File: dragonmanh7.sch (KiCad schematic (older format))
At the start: 113 parts, among them J1 USB_B, J10 Conn_02x12_Odd_Even, J11 Conn_02x03_Odd_Even, J12 VBAT+, J13 Conn_02x05_Odd_Even, J14 VBATG, J15 Conn_02x02_Odd_Even, J18 Conn_02x05_Odd_Even, J2 73725-0110BLF, J3 RJ45_Amphenol_RJMG1BD3B8K1ANR, J4 Micro_SD_Card, J5 Screw_Terminal_01x06, J6 Conn_02x12_Odd_Even, J7 USB_B, J8 Screw_Terminal_01x02, J9 Conn_02x12_Odd_Even, SW1 RESET, SW2 PC13, U1 STM32H743VITx, U10 USBLC6-2SC6, U12 TCAN332, U13 ISL83483, U14 MIC2005A, U2 KSZ8081RNA, U5 S25FL127SABMFI101, U6 AP63203, U7 USBLC6-2SC6, U8 STM32F042F6Px, U9 USBLC6-2SC6, Y1 8MHz, Y2 32.768KHz, Y3 25MHz

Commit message: Add voltage testpoints
Signed-off-by: Martin Alejandro Ribelotta <martinribelotta@gmail.com>
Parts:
- added TP1: VBAT_TP, TestPoint:TestPoint_Pad_D2.5mm, symbol Connector:TestPoint_Probe
- added TP2: VBUS1_TP, TestPoint:TestPoint_Pad_D2.5mm, symbol Connector:TestPoint_Probe
- added TP3: VBUS2_TP, TestPoint:TestPoint_Pad_D2.5mm, symbol Connector:TestPoint_Probe
- added TP4: VBUS3_TP, TestPoint:TestPoint_Pad_D2.5mm, symbol Connector:TestPoint_Probe
- added TP5: VIN_TP, TestPoint:TestPoint_Pad_D2.5mm, symbol Connector:TestPoint_Probe
- added TP6: 3V3_TP, TestPoint:TestPoint_Pad_D2.5mm, symbol Connector:TestPoint_Probe
- U8: symbol dragonmanh7-rescue:STM32F042F4Px-MCU_ST_STM32F0 -> dragonmanh7-rescue:STM32F042F4Px-MCU_ST_STM32F0-dragonmanh7-rescue
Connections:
- wire segments 246 -> 252
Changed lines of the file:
@@
 	1250 8400 1350 8400
 $Comp
-L dragonmanh7-rescue:STM32F042F4Px-MCU_ST_STM32F0 U8
+L dragonmanh7-rescue:STM32F042F4Px-MCU_ST_STM32F0-dragonmanh7-rescue U8
 U 1 1 5C7F1703
 P 14650 1800
@@
 	1    0    0    -1
 $EndComp
+$Comp
+L Connector:TestPoint_Probe TP6
+U 1 1 5E1CFBDB
+P 15200 8200
+F 0 "TP6" H 15352 8301 50  0000 L CNN
+F 1 "3V3_TP" H 15352 8210 50  0000 L CNN
+F 2 "TestPoint:TestPoint_Pad_D2.5mm" H 15400 8200 50  0001 C CNN
+F 3 "~" H 15400 8200 50  0001 C CNN
+	1    15200 8200
+	1    0    0    -1
+$EndComp
+Connection ~ 15100 8200
+Wire Wire Line
+	15100 8200 15200 8200
+$Comp
+L Connector:TestPoint_Probe TP5
+U 1 1 5E1E58CC
+P 14000 8050
+F 0 "TP5" H 14153 8151 50  0000 L CNN
+F 1 "VIN_TP" H 14153 8060 50  0000 L CNN
+F 2 "TestPoint:TestPoint_Pad_D2.5mm" H 14200 8050 50  0001 C CNN
+F 3 "~" H 14200 8050 50  0001 C CNN
+	1    14000 8050
+	1    0    0    -1
+$EndComp
+Wire Wire Line
+	14000 8050 13850 8050
+$Comp
+L Connector:TestPoint_Probe TP3
+U 1 1 5E1FA9DD
+P 7950 4850
+F 0 "TP3" H 8005 5140 50  0000 C CNN
+F 1 "VBUS2_TP" H 8005 5049 50  0000 C CNN
+F 2 "TestPoint:TestPoint_Pad_D2.5mm" H 8150 4850 50  0001 C CNN
+F 3 "~" H 8150 4850 50  0001 C CNN
+	1    7950 4850
+	-1   0    0    -1
+$EndComp
+Wire Wire Line
+	7950 4850 8300 4850
+$Comp
+L Connector:TestPoint_Probe TP2
+U 1 1 5E213482
+P 7950 3600
+F 0 "TP2" H 8005 3890 50  0000 C CNN
+F 1 "VBUS1_TP" H 8005 3799 50  0000 C CNN
+F 2 "TestPoint:TestPoint_Pad_D2.5mm" H 8150 3600 50  0001 C CNN
+F 3 "~" H 8150 3600 50  0001 C CNN
+	1    7950 3600
+	-1   0    0    -1
+$EndComp
+Wire Wire Line
+	8350 3600 7950 3600
+$Comp
+L Connector:TestPoint_Probe TP4
+U 1 1 5E228BB0
+P 8050 6400
+F 0 "TP4" H 8203 6408 50  0000 L CNN
+F 1 "VBUS3_TP" H 8203 6499 50  0000 L CNN
+F 2 "TestPoint:TestPoint_Pad_D2.5mm" H 8250 6400 50  0001 C CNN
+F 3 "~" H 8250 6400 50  0001 C CNN
+	1    8050 6400
+	-1   0    0    1
+$EndComp
+Wire Wire Line
+	8050 6400 8400 6400
+$Comp
+L Connector:TestPoint_Probe TP1
+U 1 1 5E2616EE
+P 1000 5400
+F 0 "TP1" H 1055 5690 50  0000 C CNN
+F 1 "VBAT_TP" H 1055 5599 50  0000 C CNN
+F 2 "TestPoint:TestPoint_Pad_D2.5mm" H 1200 5400 50  0001 C CNN
+F 3 "~" H 1200 5400 50  0001 C CNN
+	1    1000 5400
+	-1   0    0    -1
+$EndComp
+$Comp
+L power:+BATT #PWR0127
+U 1 1 5E26B945
+P 1150 5400
+F 0 "#PWR0127" H 1150 5250 50  0001 C CNN
+F 1 "+BATT" V 1165 5527 50  0000 L CNN
+F 2 "" H 1150 5400 50  0001 C CNN
+F 3 "" H 1150 5400 50  0001 C CNN
+	1    1150 5400
+	0    1    1    0
+$EndComp
+Wire Wire Line
+	1150 5400 1000 5400
 $EndSCHEMATC

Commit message: Change PHY to LAN8742 and change power scheme to improve 5V handling
Signed-off-by: Martin Ribelotta <martinribelotta@gmail.com>
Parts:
- removed J1, J7: USB_B, Connector_USB:USB_B_OST_USB-B1HSxx_Horizontal, symbol Connector:USB_B
- removed J11: Conn_02x03_Odd_Even, Connector_PinHeader_2.54mm:PinHeader_2x03_P2.54mm_Vertical, symbol Connector_Generic:Conn_02x03_Odd_Even
- removed U2: KSZ8081RNA, Package_DFN_QFN:QFN-24-1EP_4x4mm_P0.5mm_EP2.6x2.6mm, symbol Interface_Ethernet:KSZ8081RNA
- added C36: 0.1u, Capacitor_SMD:C_0603_1608Metric, symbol Device:C_Small
- added C37, C38: 2.2u, Capacitor_SMD:C_0805_2012Metric, symbol Device:C_Small
- added D3: ABS6UTR, Diode_SMD:Diode_Bridge_Diotec_ABS, symbol Diode_Bridge:ABS2
- added FB1: Ferrite_Bead, Inductor_SMD:L_0603_1608Metric, symbol Device:Ferrite_Bead
- added J1, J7: USB_C, Connector_USB:USB_C_Receptacle_Palconn_UTC16-G, symbol Connector:USB_C_Receptacle_USB2.0
- added J11: Conn_02x05_Odd_Even, Connector_PinSocket_2.54mm:PinSocket_2x05_P2.54mm_Vertical, symbol Connector_Generic:Conn_02x05_Odd_Even
- added JP3: BOOTB, Connector_PinHeader_2.54mm:PinHeader_1x02_P2.54mm_Vertical, symbol Device:Jumper_NC_Small
- added R25, R27, R29: 33R, Resistor_SMD:R_0603_1608Metric, symbol Device:R_Small
- added R26, R28, R30, R31, R36: 10K, Resistor_SMD:R_0603_1608Metric, symbol Device:R_Small
- added R32, R33, R34, R35: 49.9R, Resistor_SMD:R_0603_1608Metric, symbol Device:R_Small
- added R37: 220R, Resistor_SMD:R_0603_1608Metric, symbol Device:R_Small
- added R38, R39, R40, R41: 5K1, Resistor_SMD:R_0603_1608Metric, symbol Device:R_Small
- added TP7: M0-SWDIO, TestPoint:TestPoint_Pad_1.0x1.0mm, symbol Connector:TestPoint_Probe
- added TP8: M0-SWCLK, TestPoint:TestPoint_Pad_1.0x1.0mm, symbol Connector:TestPoint_Probe
- added TP9: M0-RST, TestPoint:TestPoint_Pad_1.0x1.0mm, symbol Connector:TestPoint_Probe
- added U2: LAN8742A-CZ-TR, footprints:Microchip-C04-143B-S4QFN-0-0-IPC_C, symbol eec:LAN8742A-CZ-TR
- added U3: AZ1117CD-3.3TRG1, Package_TO_SOT_SMD:TO-252-2, symbol Regulator_Linear:AZ1117-3.3
- C1, C10, C11, C12, C13, C14, C15, C16, C2, C20, C21, C22, C23, C24, C25, C26, C27, C28, C3, C34, C4, C43, C6, C7, C8, C9: footprint Capacitor_SMD:C_0805_2012Metric -> Capacitor_SMD:C_0603_1608Metric
- C18: value 4.7u -> 470p; footprint Capacitor_SMD:C_0805_2012Metric -> Capacitor_SMD:C_0603_1608Metric
- C19, C5: value 4.7u -> 10u
- C32, C33: value 22p -> 30p; footprint Capacitor_SMD:C_0805_2012Metric -> Capacitor_SMD:C_0603_1608Metric
- C35: value 0.1u -> 22n; footprint Capacitor_SMD:C_0805_2012Metric -> Capacitor_SMD:C_0603_1608Metric
- D2, D4, D5: value B120-E3 -> MBR120VLSFT3G; footprint Diode_SMD:D_SOD-123 -> Diode_SMD:D_SOD-123F
- L1: value 68uH -> 4.7u; manf# 1255AY-3R9N=P3 -> 1255AY-4R7M=P3
- R1, R10, R11, R12, R13, R14, R15, R16, R17, R18, R19, R2, R20, R21, R22, R23, R24, R3, R7, R8, R9: footprint Resistor_SMD:R_0805_2012Metric -> Resistor_SMD:R_0603_1608Metric
- R4: value 4K7 -> 33R; footprint Resistor_SMD:R_0805_2012Metric -> Resistor_SMD:R_0603_1608Metric; manf# RC0805JR-074K7L -> CRGCQ0805J22R
- R5: value 4K7 -> 10K; footprint Resistor_SMD:R_0805_2012Metric -> Resistor_SMD:R_0603_1608Metric
- R6: value 6.49K 1% -> 12K1; footprint Resistor_SMD:R_0805_2012Metric -> Resistor_SMD:R_0603_1608Metric
- U10, U7, U9: symbol Power_Protection:USBLC6-2SC6 -> dragonmanh7-rescue:USBLC6-2SC6-Power_Protection
- U6: value AP63203 -> AP63205
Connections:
- net labels added: +5V, 1V8ETH, PHY_CRS_DV, PHY_RXD0, PHY_RXD1, VDDETH, VDINA, VDINB, ~ETH_RST
- net labels removed: ETH_LED
- wire segments 252 -> 364
- no-connect marks 8 -> 10
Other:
- moved on the sheet: C17, C18, C19, C20, C21, C23, C28, C29, C30, C31, C32, C33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

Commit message: Improve schematic and PCB
Signed-off-by: Martin Ribelotta <martinribelotta@gmail.com>
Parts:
- added J16: Conn_02x02_Odd_Even, Connector_PinSocket_2.54mm:PinSocket_2x02_P2.54mm_Vertical, symbol Connector_Generic:Conn_02x02_Odd_Even
- added TP10: VDC_TP, TestPoint:TestPoint_Pad_D2.5mm, symbol Connector:TestPoint_Probe
- added TP11: 5V_TP, TestPoint:TestPoint_Pad_D2.5mm, symbol Connector:TestPoint_Probe
- J1, J7: symbol Connector:USB_C_Receptacle_USB2.0 -> dragonmanh7-rescue:USB_C_Receptacle_USB2.0-Connector
- J6: footprint Connector_PinSocket_2.54mm:PinSocket_2x12_P2.54mm_Vertical -> Connector_PinSocket_2.54mm:PinSocket_2x08_P2.54mm_Vertical; symbol Connector_Generic:Conn_02x12_Odd_Even -> Connector_Generic:Conn_02x08_Odd_Even
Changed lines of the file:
@@
 Text Label 3750 6250 0    50   ~ 0
 PC13
-Text Label 1150 10000 2    50   ~ 0
+Text Label 1150 9900 2    50   ~ 0
 PD8
-Text Label 1650 10000 0    50   ~ 0
+Text Label 1650 9900 0    50   ~ 0
 PD9
-Text Label 1150 10100 2    50   ~ 0
+Text Label 1150 10000 2    50   ~ 0
 PD10
-Text Label 1650 10100 0    50   ~ 0
+Text Label 1650 10000 0    50   ~ 0
 PD11
-Text Label 1150 10200 2    50   ~ 0
+Text Label 1150 10100 2    50   ~ 0
 PD12
-Text Label 1650 10200 0    50   ~ 0
+Text Label 1650 10100 0    50   ~ 0
 PD13
-Text Label 1150 10300 2    50   ~ 0
+Text Label 1150 10200 2    50   ~ 0
 PD14
-Text Label 1650 10300 0    50   ~ 0
+Text Label 1650 10200 0    50   ~ 0
 PD15
-Text Label 1150 10400 2    50   ~ 0
+Text Label 1150 10300 2    50   ~ 0
 PC6
-Text Label 1650 10400 0    50   ~ 0
+Text Label 1650 10300 0    50   ~ 0
 PC7
-Text Label 1150 10500 2    50   ~ 0
+Text Label 1150 10400 2    50   ~ 0
 PC9
-Text Label 1650 10500 0    50   ~ 0
+Text Label 1650 10400 0    50   ~ 0
 PA8
-Text Label 1650 9900 0    50   ~ 0
+Text Label 1650 9800 0    50   ~ 0
 PB10
 Text Label 1150 9700 2    50   ~ 0
-PE11
-Text Label 1650 9700 0    50   ~ 0
-PE12
-Text Label 1150 9800 2    50   ~ 0
 PE13
-Text Label 1650 9800 0    50   ~ 0
+Text Label 1650 9700 0    50   ~ 0
 PE14
-Text Label 1150 9900 2    50   ~ 0
+Text Label 1150 9800 2    50   ~ 0
 PE15
-Wire Wire Line
-	1150 9600 1150 9500
-Wire Wire Line
-	1650 9500 1650 9600
-$Comp
-L power:GND #PWR0151
-U 1 1 5C757D5C
-P 1150 9600
-F 0 "#PWR0151" H 1150 9350 50  0001 C CNN
-F 1 "GND" V 1150 9450 50  0000 R CNN
-F 2 "" H 1150 9600 50  0001 C CNN
-F 3 "" H 1150 9600 50  0001 C CNN
-	1    1150 9600
-	0    1    1    0
-$EndComp
-$Comp
-L power:+3.3V #PWR0152
-U 1 1 5C757E97
-P 1650 9600
-F 0 "#PWR0152" H 1650 9450 50  0001 C CNN
-F 1 "+3.3V" V 1665 9728 50  0000 L CNN
-F 2 "" H 1650 9600 50  0001 C CNN
-F 3 "" H 1650 9600 50  0001 C CNN
-	1    1650 9600
-	0    1    1    0
-$EndComp
 Text Label 3800 10600 0    50   ~ 0
 PC10
@@
 	12850 9050 12850 8700
 Wire Wire Line
-	12850 8700 14050 8700
+	12850 8700 13150 8700
 Wire Wire Line
 	12850 9250 12850 9150
@@
 C_USBH_D-
 $Comp
-L Connector_Generic:Conn_02x12_Odd_Even J6
+L Connector_Generic:Conn_02x08_Odd_Even J6
 U 1 1 5C85A792
-P 1350 10100
-F 0 "J6" H 1400 9275 50  0000 C CNN
-F 1 "Conn_02x12_Odd_Even" H 1400 9366 50  0000 C CNN
-F 2 "Connector_PinSocket_2.54mm:PinSocket_2x12_P2.54mm_Vertical" H 1350 10100 50  0001 C CNN
-F 3 "~" H 1350 10100 50  0001 C CNN
-	1    1350 10100
-	1    0    0    1
+P 1450 10100
+F 0 "J6" H 1500 9275 50  0000 C CNN
+F 1 "Conn_02x12_Odd_Even" H 1500 9366 50  0000 C CNN
+F 2 "Connector_PinSocket_2.54mm:PinSocket_2x08_P2.54mm_Vertical" H 1450 10100 50  0001 C CNN
+F 3 "~" H 1450 10100 50  0001 C CNN
+	1    1450 10100
+	-1   0    0    1
 $EndComp
-Text Label 1150 10600 2    50   ~ 0
+Text Label 4350 8950 0    50   ~ 0
 U1_TX
-Text Label 1650 10600 0    50   ~ 0
+Text Label 4350 8850 0    50   ~ 0
 U1_RX
 Wire Wire Line
@@
 Wire Wire Line
 	2800 10500 2800 10600
-Connection ~ 1650 9600
-Connection ~ 1150 9600
 Connection ~ 1450 7900
 Wire Wire Line
@@
 $EndComp
 $Comp
-L Connector:USB_C_Receptacle_USB2.0 J7
+L dragonmanh7-rescue:USB_C_Receptacle_USB2.0-Connector J7
 U 1 1 611E4C9F
 P 11450 3950
@@
 	10850 1450 10850 1550
 $Comp
-L Connector:USB_C_Receptacle_USB2.0 J1
+L dragonmanh7-rescue:USB_C_Receptacle_USB2.0-Connector J1
 U 1 1 60FA9730
 P 11450 1550
@@
 	14400 8300 14650 8300
 Wire Wire Line
-	14650 8300 14650 8500
+	14650 8300 14650 8400
 Wire Wire Line
 	14650 8700 14400 8700
@@
 Wire Wire Line
 	12200 8750 12200 8850
+$Comp
+L Connector_Generic:Conn_02x02_Odd_Even J16
+U 1 1 5FB285DF
+P 4150 8950
+F 0 "J16" H 4200 8625 50  0000 C CNN
+F 1 "Conn_02x02_Odd_Even" H 4200 8716 50  0000 C CNN
+F 2 "Connector_PinSocket_2.54mm:PinSocket_2x02_P2.54mm_Vertical" H 4150 8950 50  0001 C CNN
+F 3 "~" H 4150 8950 50  0001 C CNN
+	1    4150 8950
+	-1   0    0    1
+$EndComp
+$Comp
+L power:GND #PWR0118
+U 1 1 5FB2EE8D
+P 3850 8950
+F 0 "#PWR0118" H 3850 8700 50  0001 C CNN
+F 1 "GND" V 3855 8822 50  0000 R CNN
+F 2 "" H 3850 8950 50  0001 C CNN
+F 3 "" H 3850 8950 50  0001 C CNN
+	1    3850 8950
+	0    1    -1   0
+$EndComp
+$Comp
+L power:+3.3V #PWR0128
+U 1 1 5FB2F9D8
+P 3850 8850
+F 0 "#PWR0128" H 3850 8700 50  0001 C CNN
+F 1 "+3.3V" V 3865 8978 50  0000 L CNN
+F 2 "" H 3850 8850 50  0001 C CNN
+F 3 "" H 3850 8850 50  0001 C CNN
+	1    3850 8850
+	0    -1   -1   0
+$EndComp
+$Comp
+L Connector:TestPoint_Probe TP11
+U 1 1 5FA637E6
+P 14650 8400
+F 0 "TP11" H 14802 8501 50  0000 L CNN
+F 1 "5V_TP" H 14802 8410 50  0000 L CNN
+F 2 "TestPoint:TestPoint_Pad_D2.5mm" H 14850 8400 50  0001 C CNN
+F 3 "~" H 14850 8400 50  0001 C CNN
+	1    14650 8400
+	1    0    0    -1
+$EndComp
+Connection ~ 14650 8400
+Wire Wire Line
+	14650 8400 14650 8500
+$Comp
+L Connector:TestPoint_Probe TP10
+U 1 1 5FA6AA05
+P 13150 8700
+F 0 "TP10" V 13440 8755 50  0000 C CNN
+F 1 "VDC_TP" V 13349 8755 50  0000 C CNN
+F 2 "TestPoint:TestPoint_Pad_D2.5mm" H 13350 8700 50  0001 C CNN
+F 3 "~" H 13350 8700 50  0001 C CNN
+	1    13150 8700
+	0    -1   -1   0
+$EndComp
+Connection ~ 13150 8700
+Wire Wire Line
+	13150 8700 14050 8700
 $EndSCHEMATC

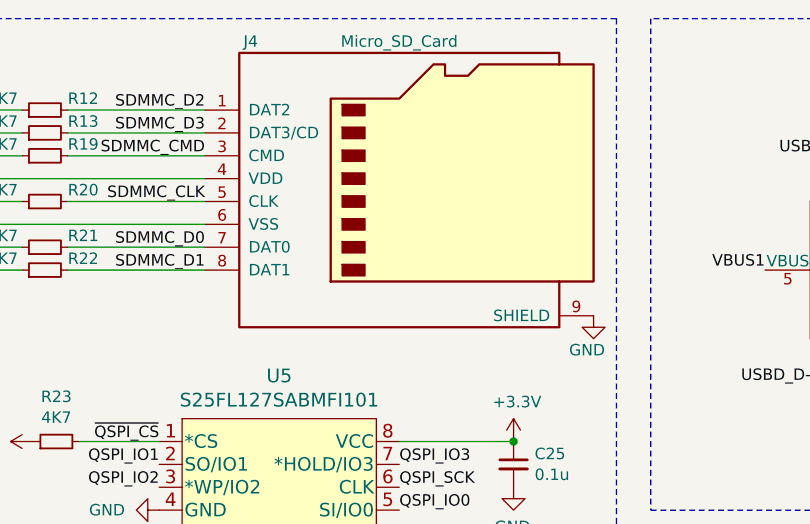
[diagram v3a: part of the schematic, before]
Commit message: Change uSD card connector by Molex 1051620001
Signed-off-by: Martin Ribelotta <martinribelotta@gmail.com>
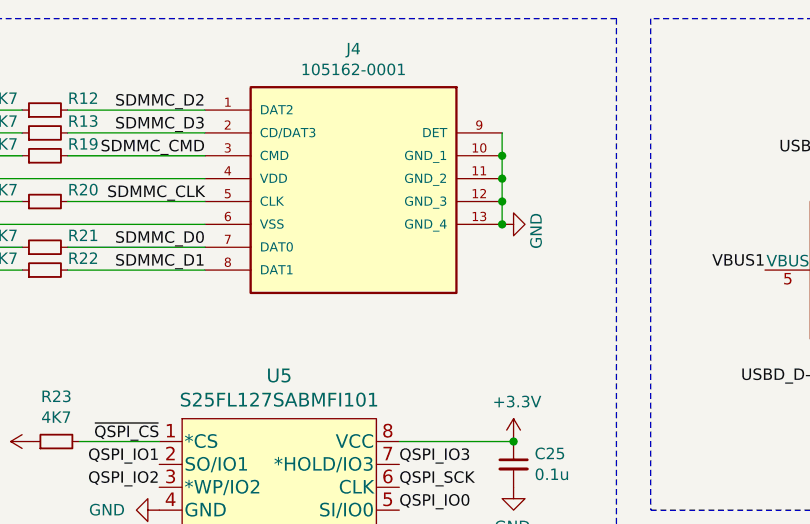
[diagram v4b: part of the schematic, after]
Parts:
- removed J4: Micro_SD_Card, Connector_Card:microSD_HC_Hirose_DM3D-SF, symbol Connector:Micro_SD_Card
- added J4: 105162-0001, footprints:105162-0001, symbol 105162-0001:105162-0001
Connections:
- net +3V3: now also J4.4 (VDD)
- net GND: now also J4.10 (GND_1), J4.11 (GND_2), J4.12 (GND_3), J4.13 (GND_4), J4.6 (VSS), J4.9 (DET)
- net SDMMC_CLK: now also J4.5 (CLK)
- net SDMMC_CMD: now also J4.3 (CMD)
- net SDMMC_D0: now also J4.7 (DAT0)
- net SDMMC_D1: now also J4.8 (DAT1)
- net SDMMC_D2: now also J4.1 (DAT2)
- net SDMMC_D3: now also J4.2 (CD/DAT3)
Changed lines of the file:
@@
 L power:GND #PWR0124
 U 1 1 5C65D59B
-P 8250 1850
-F 0 "#PWR0124" H 8250 1600 50  0001 C CNN
-F 1 "GND" H 8300 1700 50  0000 R CNN
-F 2 "" H 8250 1850 50  0001 C CNN
-F 3 "" H 8250 1850 50  0001 C CNN
-	1    8250 1850
-	1    0    0    -1
+P 7850 1450
+F 0 "#PWR0124" H 7850 1200 50  0001 C CNN
+F 1 "GND" H 7900 1300 50  0000 R CNN
+F 2 "" H 7850 1450 50  0001 C CNN
+F 3 "" H 7850 1450 50  0001 C CNN
+	1    7850 1450
+	0    -1   -1   0
 $EndComp
 Text Label 1950 5050 2    50   ~ 0
@@
 	0    -1   -1   0
 $EndComp
-$Comp
-L Connector:Micro_SD_Card J4
-U 1 1 5D206CAA
-P 7450 1250
-F 0 "J4" H 6750 1850 50  0000 C CNN
-F 1 "Micro_SD_Card" H 7400 1850 50  0000 C CNN
-F 2 "Connector_Card:microSD_HC_Hirose_DM3D-SF" H 8600 1550 50  0001 C CNN
-F 3 "http://katalog.we-online.de/em/datasheet/693072010801.pdf" H 7450 1250 50  0001 C CNN
-	1    7450 1250
-	1    0    0    -1
-$EndComp
 Wire Wire Line
 	5950 1650 6550 1650
@@
 Wire Wire Line
 	13150 8700 14050 8700
+$Comp
+L 105162-0001:105162-0001 J4
+U 1 1 5FA74A6B
+P 6550 950
+F 0 "J4" H 7200 1217 50  0000 C CNN
+F 1 "105162-0001" H 7200 1126 50  0000 C CNN
+F 2 "footprints:105162-0001" H 6550 950 50  0001 L BNN
+F 3 "" H 6550 950 50  0001 L BNN
+F 4 "https://www.mouser.co.uk/ProductDetail/Molex/105162-0001?qs=1fNsfHe5VsK8daqlgKxZfQ%3D%3D" H 6550 950 50  0001 L BNN "MOUSER_PRICE-STOCK"
+F 5 "105162-0001" H 6550 950 50  0001 L BNN "MANUFACTURER_PART_NUMBER"
+F 6 "538-105162-0001" H 6550 950 50  0001 L BNN "MOUSER_PART_NUMBER"
+F 7 "Molex" H 6550 950 50  0001 L BNN "MANUFACTURER_NAME"
+F 8 "Memory Card Connectors 1.45H MICRO SD HEADER WITH D/C PIN" H 6550 950 50  0001 L BNN "DESCRIPTION"
+F 9 "mm" H 6550 950 50  0001 L BNN "HEIGHT"
+	1    6550 950
+	1    0    0    -1
+$EndComp
+Wire Wire Line
+	7850 1150 7850 1250
+Connection ~ 7850 1450
+Connection ~ 7850 1250
+Wire Wire Line
+	7850 1250 7850 1350
+Connection ~ 7850 1350
+Wire Wire Line
+	7850 1350 7850 1450
+Wire Wire Line
+	7850 1050 7850 1150
+Connection ~ 7850 1150
 $EndSCHEMATC
